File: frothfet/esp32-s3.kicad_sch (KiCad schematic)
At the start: 47 parts, among them J3 USB_TYPE_C_16PIN, Q20 FDC6330L, Q21 S8050, Q22 S8050, SW1 RESET, SW2 BOOT, U31 ESP32-S3-WROOM-1-N16R8, U32 USBLC6-2SC6, U33 XC6210B332MR, U34 CH334F, U35 CH343P, Y1 12Mhz, Y2 32.768kHz

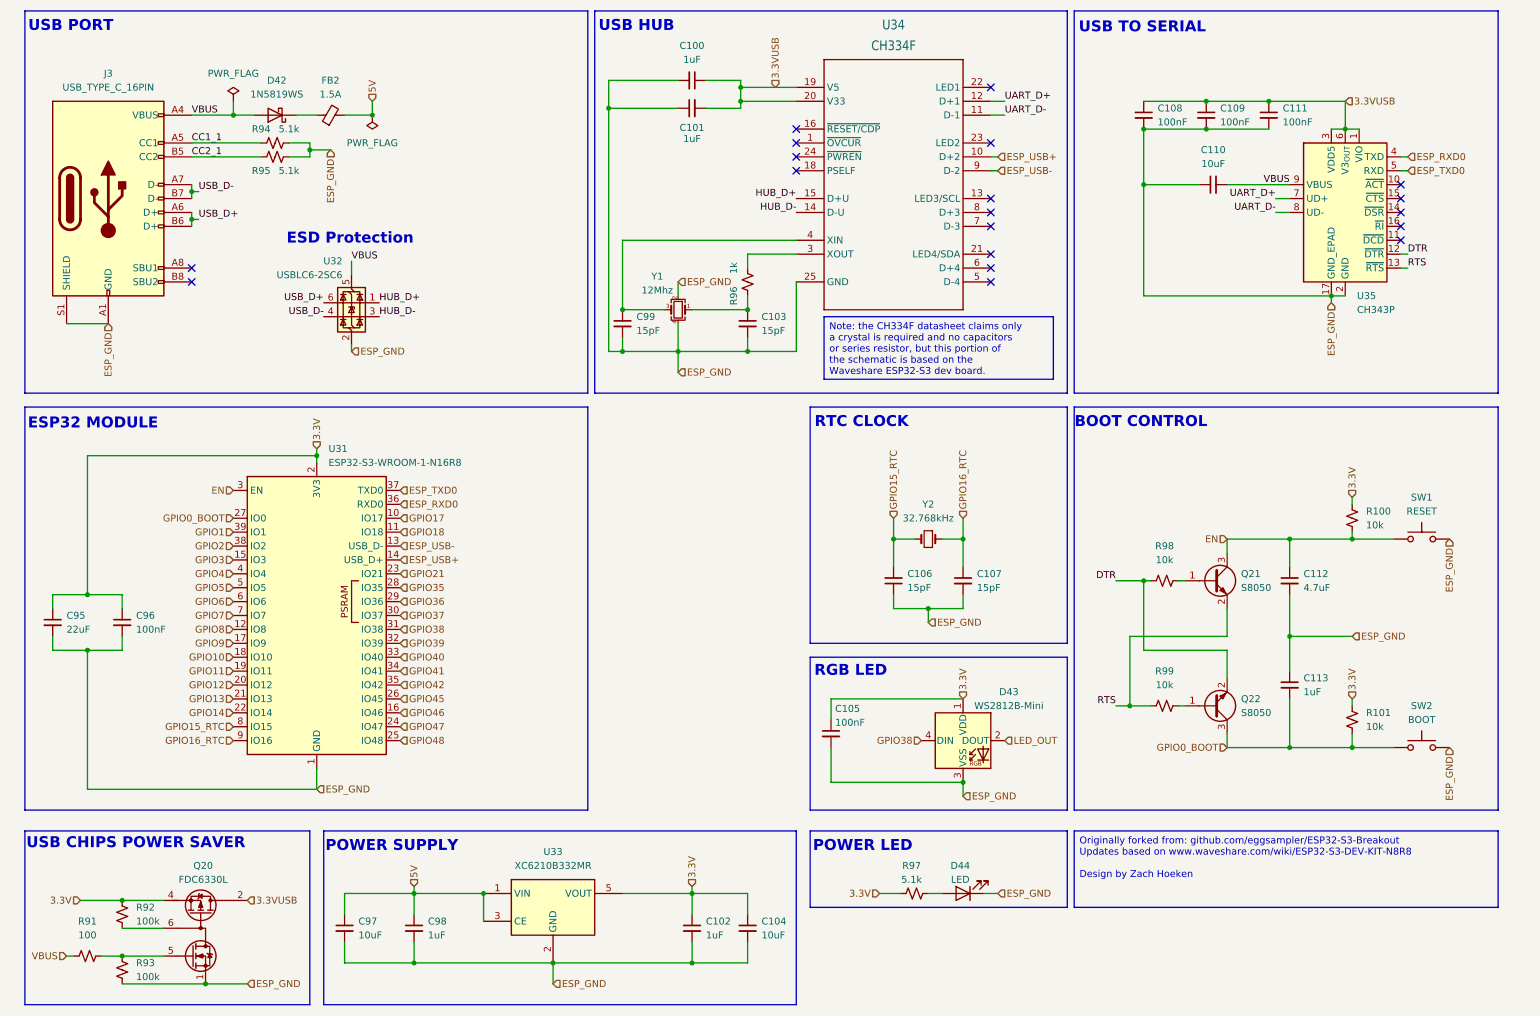
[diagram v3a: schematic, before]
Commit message: imported latest esp32-s3 module
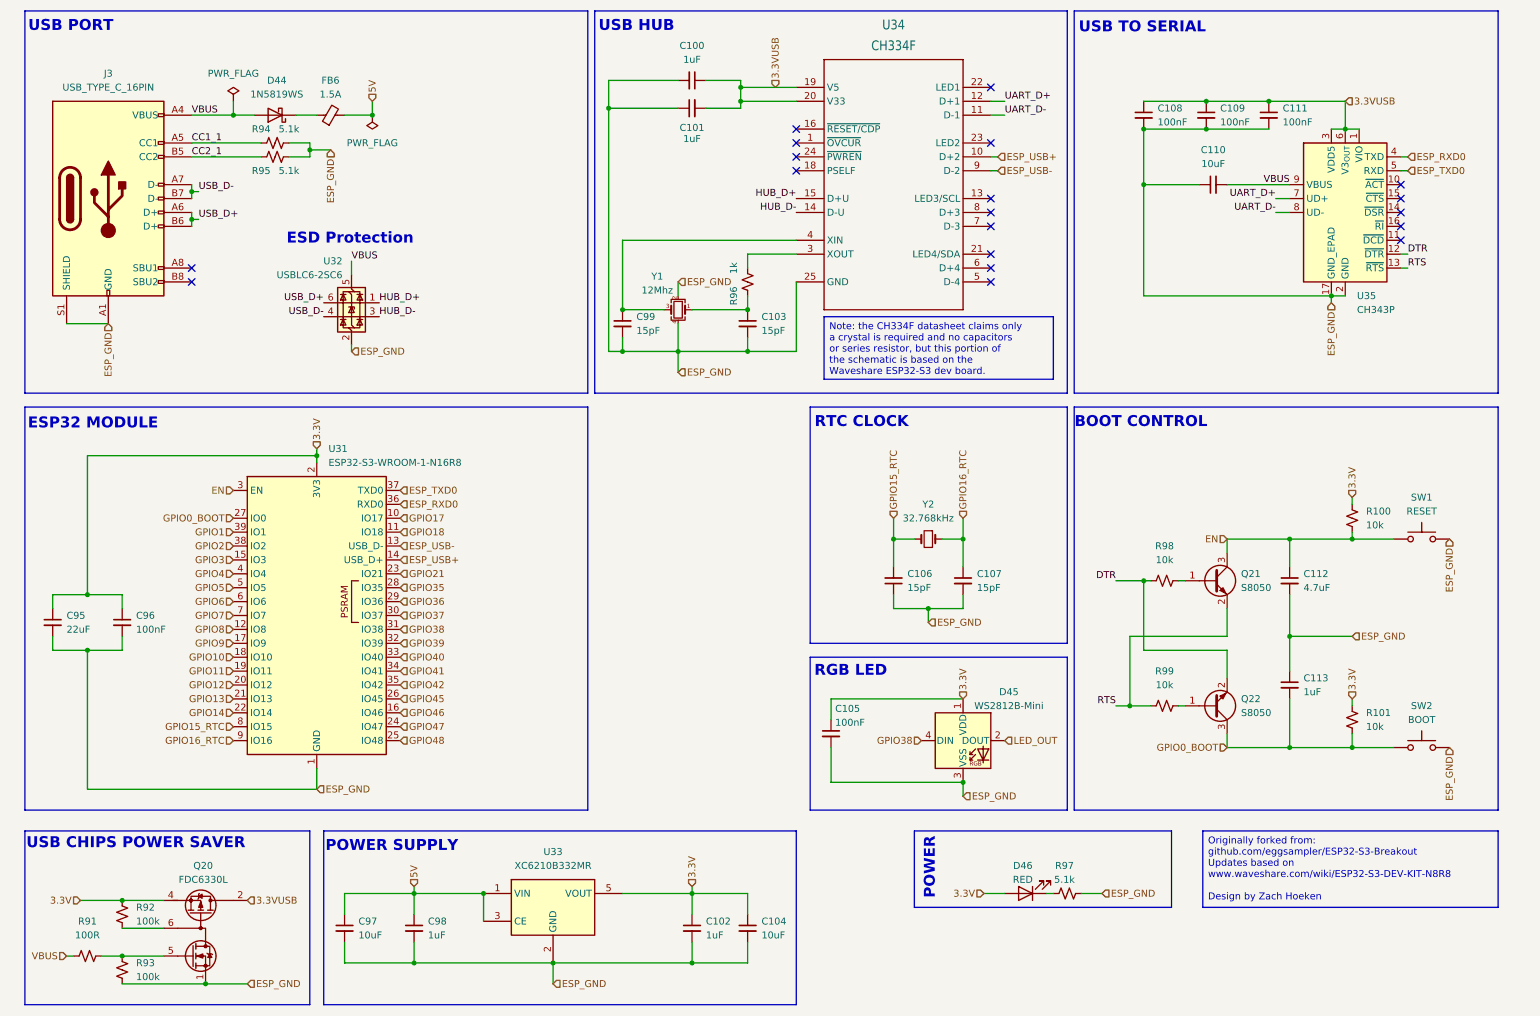
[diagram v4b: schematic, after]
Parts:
- D44: renamed from D42; LCSC (none) -> C191023
- D46: renamed from D44; value LED -> RED; LCSC C2286 -> C965799
- J3: Position Offset (none) -> 0.0,1.27
- Q20: LCSC (none) -> C112086
- R91: value 100 -> 100R
- SW1, SW2: LCSC C843684 -> C557599; Rotation Offset (none) -> 180
- U31: footprint RF_Module:ESP32-S3-WROOM-1 -> yarrboard:ESP32-S3-WROOM-1; LCSC (none) -> C2913202; Position Offset (none) -> 0,-3.6195
- U32: Rotation Offset (none) -> 90
- U33: LCSC (none) -> C424705
- U34: footprint Package_DFN_QFN:QFN-24-1EP_4x4mm_P0.5mm_EP2.7x2.7mm_ThermalVias -> yarrboard:QFN-24-1EP_4x4mm_P0.5mm_EP2.7x2.7mm_ThermalVias; LCSC (none) -> C5187527; Rotation Offset (none) -> 180
- U35: footprint Package_DFN_QFN:QFN-16-1EP_3x3mm_P0.5mm_EP1.7x1.7mm_ThermalVias -> yarrboard:QFN-16-1EP_3x3mm_P0.5mm_EP1.7x1.7mm_ThermalVias; LCSC (none) -> C2846043; Rotation Offset (none) -> 180
- renumbered D43 to D45, FB2 to FB6
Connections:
- net 3.3V: now also D46.2 (A); no longer R97.1
- net ESP_GND: now also R97.2; no longer D46.1 (K)
- new net: D46.1 (K), R97.1
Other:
- note added: "POWER"
- note removed: "POWER LED"
- moved on the sheet: D46, R97

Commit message: about 50% routed
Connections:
- net 3.3V: now also R97.1; no longer D46.2 (A)
- net ESP_GND: now also D46.1 (K); no longer R97.2
- new net: D46.2 (A), R97.2
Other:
- moved on the sheet: D46, R97
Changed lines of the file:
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@@
 	(wire
 		(pts
-			(xy 189.23 175.26) (xy 193.04 175.26)
+			(xy 189.23 175.26) (xy 194.31 175.26)
 		)
 		(stroke
@@
 	(wire
 		(pts
+			(xy 208.28 175.26) (xy 210.82 175.26)
+		)
+		(stroke
+			(width 0)
+			(type default)
+		)
+	)
+	(wire
+		(pts
 			(xy 44.45 45.72) (xy 44.45 46.99)
 		)
@@
 	(wire
 		(pts
-			(xy 200.66 175.26) (xy 201.93 175.26)
+			(xy 199.39 175.26) (xy 200.66 175.26)
 		)
 		(stroke
@@
 	(wire
 		(pts
-			(xy 207.01 175.26) (xy 210.82 175.26)
-		)
-		(stroke
-			(width 0)
-			(type default)
-		)
-	)
-	(wire
-		(pts
 			(xy 44.45 52.07) (xy 44.45 53.34)
 		)
@@
 	(symbol
 		(lib_id "Device:LED")
-		(at 196.85 175.26 180)
+		(at 204.47 175.26 180)
 		(unit 1)
 		(exclude_from_sim no)
@@
 		(dnp no)
 		(property "Reference" "D46"
-			(at 196.342 170.18 0)
+			(at 203.962 170.18 0)
 			(effects
 				(font
@@
 		)
 		(property "Value" "RED"
-			(at 196.342 172.72 0)
+			(at 203.962 172.72 0)
 			(effects
 				(font
@@
 		)
 		(property "Footprint" "LED_SMD:LED_0603_1608Metric"
-			(at 196.85 175.26 0)
+			(at 204.47 175.26 0)
 			(effects
 				(font
@@
 		)
 		(property "Datasheet" "~"
-			(at 196.85 175.26 0)
+			(at 204.47 175.26 0)
 			(effects
 				(font
@@
 		)
 		(property "Description" "Light emitting diode"
-			(at 196.85 175.26 0)
+			(at 204.47 175.26 0)
 			(effects
 				(font
@@
 		)
 		(property "Sim.Pins" "1=K 2=A"
-			(at 196.85 175.26 0)
+			(at 204.47 175.26 0)
 			(effects
 				(font
@@
 		)
 		(property "LCSC" "C965799"
-			(at 196.85 175.26 0)
+			(at 204.47 175.26 0)
 			(effects
 				(font
@@
 	(symbol
 		(lib_id "Device:R_Small_US")
-		(at 204.47 175.26 90)
+		(at 196.85 175.26 90)
 		(unit 1)
 		(exclude_from_sim no)
@@
 		(dnp no)
 		(property "Reference" "R97"
-			(at 203.962 170.18 90)
+			(at 196.342 170.18 90)
 			(effects
 				(font
@@
 		)
 		(property "Value" "5.1k"
-			(at 203.962 172.72 90)
+			(at 196.342 172.72 90)
 			(effects
 				(font
@@
 		)
 		(property "Footprint" "Resistor_SMD:R_0603_1608Metric"
-			(at 204.47 175.26 0)
+			(at 196.85 175.26 0)
 			(effects
 				(font
@@
 		)
 		(property "Datasheet" "~"
-			(at 204.47 175.26 0)
+			(at 196.85 175.26 0)
 			(effects
 				(font
@@
 		)
 		(property "Description" "Resistor, small US symbol"
-			(at 204.47 175.26 0)
+			(at 196.85 175.26 0)
 			(effects
 				(font

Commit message: bom and placement all check out.  ready for production!
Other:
- moved on the sheet: D46, R97
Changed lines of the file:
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@@
 	)
 	(rectangle
-		(start 176.53 163.83)
-		(end 223.52 177.8)
+		(start 143.51 86.36)
+		(end 129.54 133.35)
 		(stroke
 			(width 0)
@@
 	(text "POWER"
 		(exclude_from_sim no)
-		(at 179.324 176.276 90)
+		(at 131.064 89.154 0)
 		(effects
 			(font
@@
 	(text_box "Originally forked from: github.com/eggsampler/ESP32-S3-Breakout\nUpdates based on www.waveshare.com/wiki/ESP32-S3-DEV-KIT-N8R8\n\nDesign by Zach Hoeken"
 		(exclude_from_sim no)
-		(at 229.235 163.83 0)
-		(size 53.975 13.97)
+		(at 179.705 167.64 0)
+		(size 99.695 11.43)
 		(margins 0.9525 0.9525 0.9525 0.9525)
 		(stroke
-			(width 0)
+			(width -0.0001)
 			(type solid)
 		)
@@
 	(wire
 		(pts
-			(xy 189.23 175.26) (xy 194.31 175.26)
+			(xy 132.08 99.06) (xy 132.08 104.14)
 		)
 		(stroke
@@
 	(wire
 		(pts
-			(xy 208.28 175.26) (xy 210.82 175.26)
+			(xy 132.08 118.11) (xy 132.08 120.65)
 		)
 		(stroke
@@
 	(wire
 		(pts
-			(xy 199.39 175.26) (xy 200.66 175.26)
+			(xy 132.08 109.22) (xy 132.08 110.49)
 		)
 		(stroke
@@
 	(hierarchical_label "ESP_GND"
 		(shape input)
-		(at 210.82 175.26 0)
+		(at 132.08 120.65 270)
 		(effects
 			(font
 				(size 1.27 1.27)
 			)
-			(justify left)
+			(justify right)
 		)
 	)
@@
 	(hierarchical_label "3.3V"
 		(shape input)
-		(at 189.23 175.26 180)
+		(at 132.08 99.06 90)
 		(effects
 			(font
 				(size 1.27 1.27)
 			)
-			(justify right)
+			(justify left)
 		)
 	)
@@
 	(symbol
 		(lib_id "Device:LED")
-		(at 204.47 175.26 180)
+		(at 132.08 114.3 90)
 		(unit 1)
 		(exclude_from_sim no)
@@
 		(dnp no)
 		(property "Reference" "D46"
-			(at 203.962 170.18 0)
+			(at 137.16 113.792 0)
 			(effects
 				(font
@@
 		)
 		(property "Value" "RED"
-			(at 203.962 172.72 0)
+			(at 134.62 113.792 0)
 			(effects
 				(font
@@
 		)
 		(property "Footprint" "LED_SMD:LED_0603_1608Metric"
-			(at 204.47 175.26 0)
+			(at 132.08 114.3 0)
 			(effects
 				(font
@@
 		)
 		(property "Datasheet" "~"
-			(at 204.47 175.26 0)
+			(at 132.08 114.3 0)
 			(effects
 				(font
@@
 		)
 		(property "Description" "Light emitting diode"
-			(at 204.47 175.26 0)
+			(at 132.08 114.3 0)
 			(effects
 				(font
@@
 		)
 		(property "Sim.Pins" "1=K 2=A"
-			(at 204.47 175.26 0)
+			(at 132.08 114.3 0)
 			(effects
 				(font
@@
 		)
 		(property "LCSC" "C965799"
-			(at 204.47 175.26 0)
+			(at 132.08 114.3 0)
 			(effects
 				(font
@@
 	(symbol
 		(lib_id "Device:R_Small_US")
-		(at 196.85 175.26 90)
+		(at 132.08 106.68 0)
 		(unit 1)
 		(exclude_from_sim no)
@@
 		(dnp no)
 		(property "Reference" "R97"
-			(at 196.342 170.18 90)
+			(at 137.16 106.172 90)
 			(effects
 				(font
@@
 		)
 		(property "Value" "5.1k"
-			(at 196.342 172.72 90)
+			(at 134.62 106.172 90)
 			(effects
 				(font
@@
 		)
 		(property "Footprint" "Resistor_SMD:R_0603_1608Metric"
-			(at 196.85 175.26 0)
+			(at 132.08 106.68 0)
 			(effects
 				(font
@@
 		)
 		(property "Datasheet" "~"
-			(at 196.85 175.26 0)
+			(at 132.08 106.68 0)
 			(effects
 				(font
@@
 		)
 		(property "Description" "Resistor, small US symbol"
-			(at 196.85 175.26 0)
+			(at 132.08 106.68 0)
 			(effects
 				(font
